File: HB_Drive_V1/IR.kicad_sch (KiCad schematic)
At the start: 57 parts, among them J301 Conn_02x03_Odd_Even, J303 Conn_01x02, J304 Conn_02x04_Odd_Even, U301 TL082, U302 TL082, U303 TL082, U304 TL082, U305 TL082

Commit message: updates board to REV 1 Ordered version
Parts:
- C301, C302: value 27uF 5% -> 27nF 5%
- C303: value 10uF 5% -> 10uF 10%
- R302, R308, R309, R310, R324, R325: value 10K -> 10kΩ 1%
- R307, R313, R316, R319, R322, R323, R326, R328, R329: value 10kΩ -> 10kΩ 1%
- R317: value 10KΩ -> 10kΩ 1%
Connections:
- net at R314.2, R318.2, TP301.1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: now also C301.1, R311.2
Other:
- moved on the sheet: TP301
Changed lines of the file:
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@@
 	)
 	(junction
+		(at 299.72 95.25)
+		(diameter 0)
+		(color 0 0 0 0)
+	)
+	(junction
 		(at 142.24 160.02)
 		(diameter 0)
@@
 	)
 	(junction
+		(at 325.12 107.95)
+		(diameter 0)
+		(color 0 0 0 0)
+	)
+	(junction
 		(at 124.46 160.02)
 		(diameter 0)
@@
 	(wire
 		(pts
+			(xy 299.72 95.25) (xy 320.04 95.25)
+		)
+		(stroke
+			(width 0)
+			(type default)
+		)
+	)
+	(wire
+		(pts
 			(xy 359.41 101.6) (xy 359.41 110.49)
 		)
@@
 	(wire
 		(pts
+			(xy 320.04 95.25) (xy 320.04 107.95)
+		)
+		(stroke
+			(width 0)
+			(type default)
+		)
+	)
+	(wire
+		(pts
 			(xy 314.96 78.74) (xy 331.47 78.74)
 		)
@@
 	(wire
 		(pts
+			(xy 325.12 107.95) (xy 330.2 107.95)
+		)
+		(stroke
+			(width 0)
+			(type default)
+		)
+	)
+	(wire
+		(pts
 			(xy 234.95 55.88) (xy 232.41 55.88)
 		)
@@
 	(wire
 		(pts
-			(xy 320.04 107.95) (xy 330.2 107.95)
+			(xy 320.04 107.95) (xy 325.12 107.95)
 		)
 		(stroke
@@
 			)
 		)
-		(property "Value" "10K"
+		(property "Value" "10kΩ 1%"
 			(at 129.794 101.6 90)
 			(hide yes)
@@
 			)
 		)
-		(property "Value" "10uF 5%"
+		(property "Value" "10uF 10%"
 			(at 309.118 69.85 90)
 			(show_name no)
@@
 			)
 		)
-		(property "Value" "10kΩ"
+		(property "Value" "10kΩ 1%"
 			(at 208.026 51.054 90)
 			(show_name no)
@@
 			)
 		)
-		(property "Value" "10kΩ"
-			(at 306.324 164.846 0)
+		(property "Value" "10kΩ 1%"
+			(at 308.356 164.846 0)
 			(show_name no)
 			(do_not_autoplace no)
@@
 			)
 		)
-		(property "Value" "10K"
+		(property "Value" "10kΩ 1%"
 			(at 292.354 173.99 90)
 			(hide yes)
@@
 			)
 		)
-		(property "Value" "27uF 5%"
+		(property "Value" "27nF 5%"
 			(at 292.1 99.06 90)
 			(show_name no)
@@
 			)
 		)
-		(property "Value" "10kΩ"
+		(property "Value" "10kΩ 1%"
 			(at 129.286 94.234 90)
 			(show_name no)
@@
 			)
 		)
-		(property "Value" "10K"
+		(property "Value" "10kΩ 1%"
 			(at 129.794 96.52 90)
 			(hide yes)
@@
 			)
 		)
-		(property "Value" "10kΩ"
+		(property "Value" "10kΩ 1%"
 			(at 152.146 89.154 90)
 			(show_name no)
@@
 			)
 		)
-		(property "Value" "10kΩ"
+		(property "Value" "10kΩ 1%"
 			(at 182.626 90.424 90)
 			(show_name no)
@@
 	(symbol
 		(lib_id "Connector:TestPoint")
-		(at 320.04 107.95 0)
+		(at 325.12 107.95 0)
 		(unit 1)
 		(body_style 1)
@@
 		(dnp no)
 		(property "Reference" "TP301"
-			(at 318.262 102.616 0)
+			(at 322.834 99.568 0)
 			(show_name no)
 			(do_not_autoplace no)
@@
 		)
 		(property "Value" "TestPoint"
-			(at 322.58 105.9179 0)
+			(at 327.66 105.9179 0)
 			(hide yes)
 			(show_name no)
@@
 		)
 		(property "Footprint" "TestPoint:TestPoint_Loop_D2.60mm_Drill1.6mm_Beaded"
-			(at 325.12 107.95 0)
+			(at 330.2 107.95 0)
 			(hide yes)
 			(show_name no)
@@
 		)
 		(property "Datasheet" ""
-			(at 325.12 107.95 0)
+			(at 330.2 107.95 0)
 			(hide yes)
 			(show_name no)
@@
 		)
 		(property "Description" "test point"
-			(at 320.04 107.95 0)
+			(at 325.12 107.95 0)
 			(hide yes)
 			(show_name no)
@@
 			)
 		)
-		(property "Value" "10K"
+		(property "Value" "10kΩ 1%"
 			(at 292.354 171.45 90)
 			(hide yes)
@@
 			)
 		)
-		(property "Value" "10KΩ"
+		(property "Value" "10kΩ 1%"
 			(at 163.576 52.832 90)
 			(hide yes)
@@
 			)
 		)
-		(property "Value" "27uF 5%"
+		(property "Value" "27nF 5%"
 			(at 292.1 109.22 90)
 			(show_name no)
@@
 			)
 		)
-		(property "Value" "10K"
+		(property "Value" "10kΩ 1%"
 			(at 273.304 41.91 90)
 			(show_name no)
@@
 			)
 		)
-		(property "Value" "10K"
+		(property "Value" "10kΩ 1%"
 			(at 129.794 99.06 90)
 			(hide yes)
@@
 			)
 		)
-		(property "Value" "10kΩ"
+		(property "Value" "10kΩ 1%"
 			(at 291.846 169.164 90)
 			(show_name no)
@@
 			)
 		)
-		(property "Value" "10kΩ"
+		(property "Value" "10kΩ 1%"
 			(at 224.536 43.434 90)
 			(show_name no)
@@
 			)
 		)
-		(property "Value" "10kΩ"
+		(property "Value" "10kΩ 1%"
 			(at 163.576 47.752 90)
 			(show_name no)
@@
 			)
 		)
-		(property "Value" "10kΩ"
+		(property "Value" "10kΩ 1%"
 			(at 167.386 96.774 90)
 			(show_name no)

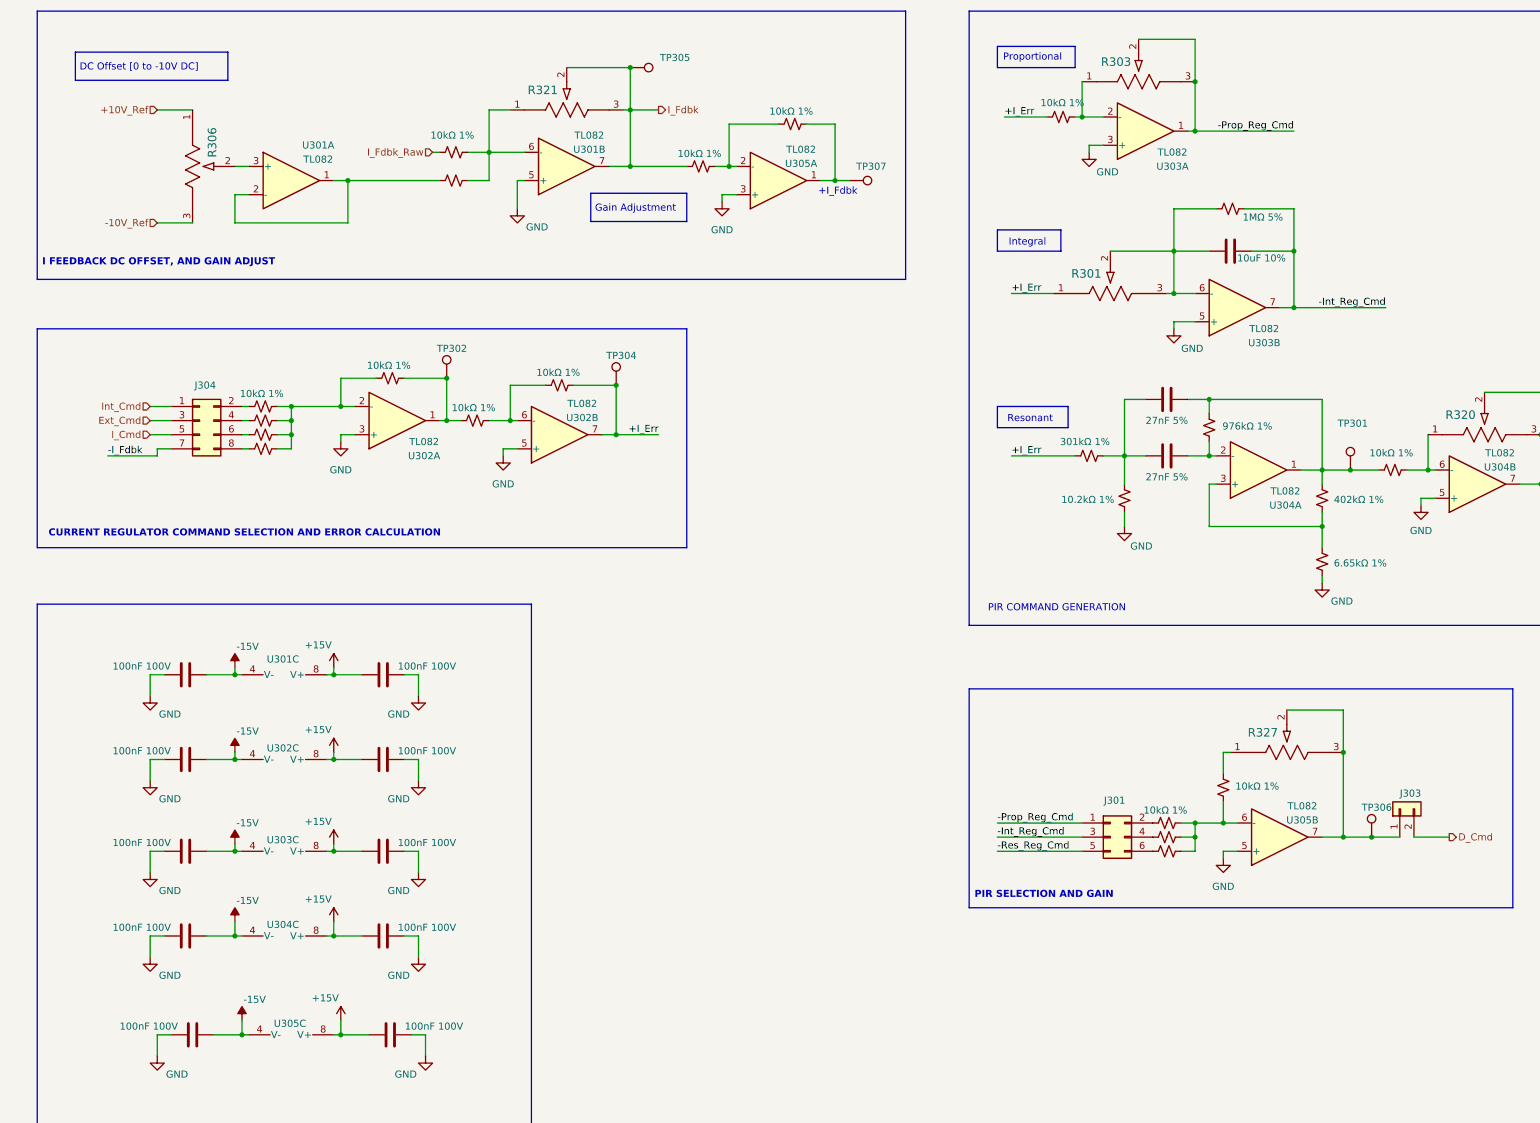
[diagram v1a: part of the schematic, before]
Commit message: Annotates Schematic! Fixes REV1 wiring swaps and replaces buffer
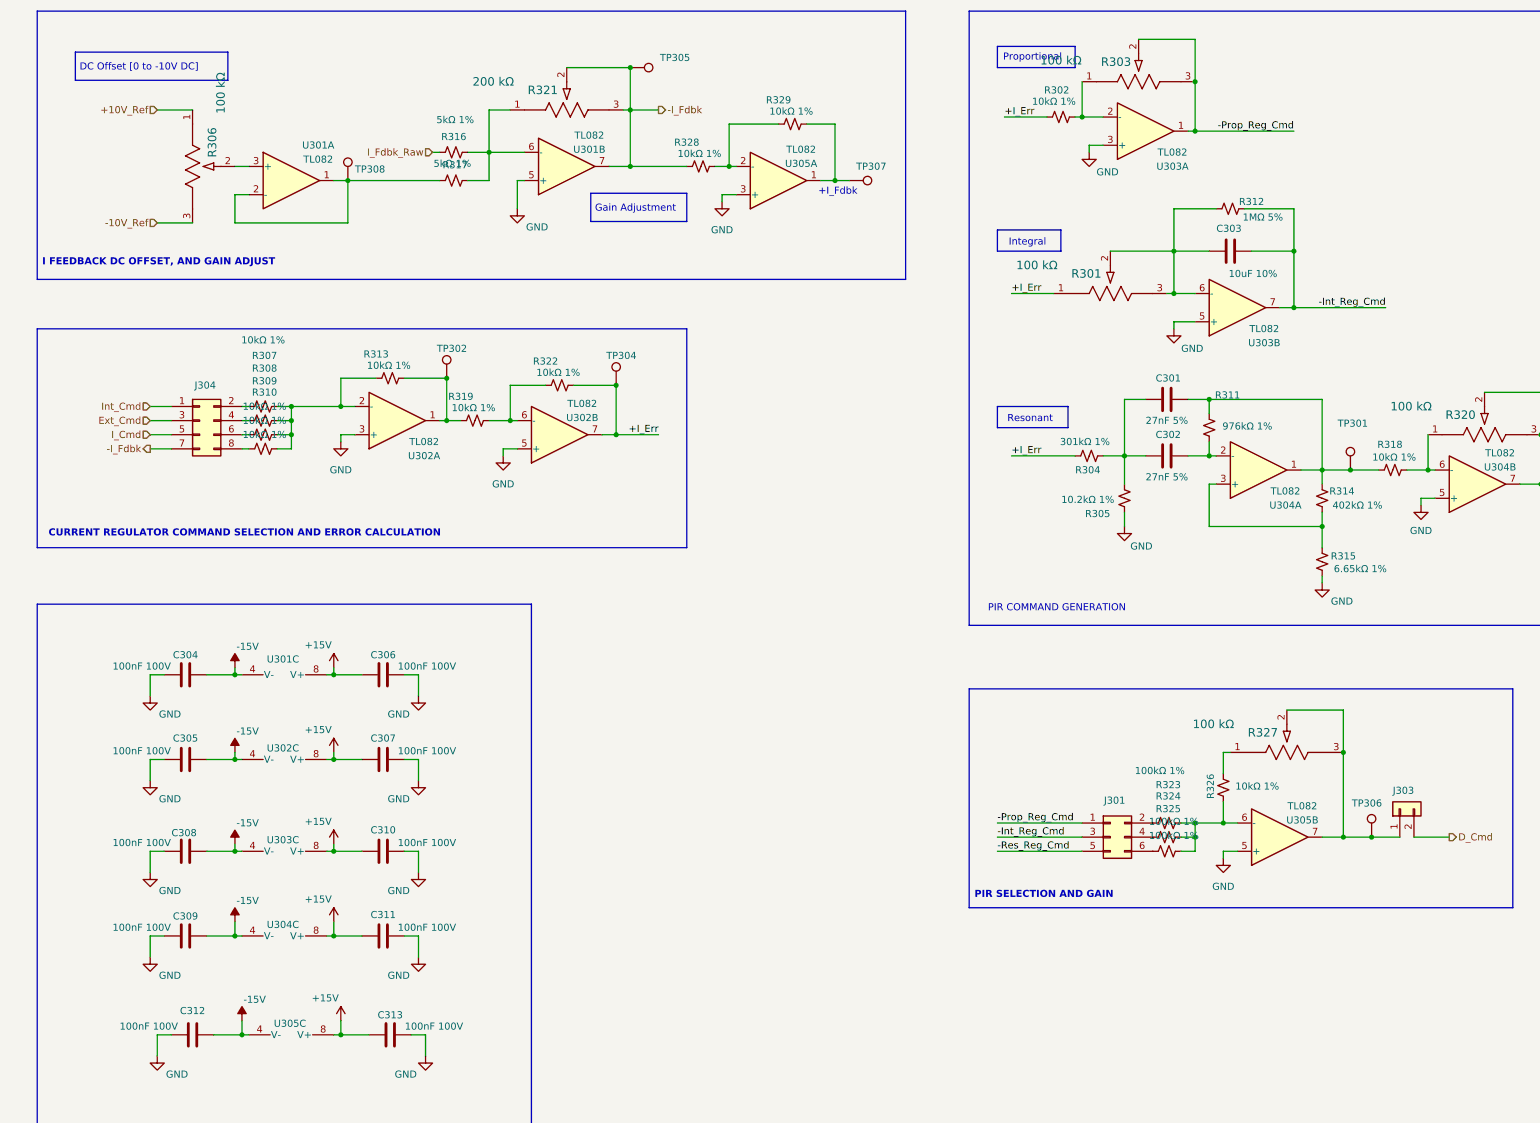
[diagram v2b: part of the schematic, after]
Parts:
- added TP308: TestPoint, TestPoint:TestPoint_Loop_D2.60mm_Drill1.6mm_Beaded, symbol Connector:TestPoint
- J303: footprint Connector_PinHeader_1.27mm:PinHeader_1x02_P1.27mm_Vertical -> Connector_PinHeader_2.54mm:PinHeader_1x02_P2.54mm_Vertical
- R301, R303, R306, R320, R327: value PV36W104C01B00 -> 100 kΩ
- R316, R317: value 10kΩ 1% -> 5kΩ 1%
- R321: value PV36W204C01B00 -> 200 kΩ
- R323, R324, R325: value 10kΩ 1% -> 100kΩ 1%
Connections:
- net I_Fdbk is gone; now on net -I_Fdbk: R321.2, R321.3, R328.2, TP305.1, U301.7
- net at R323.1, R326.1, U305.6 (-): now also R324.1, R325.1; no longer R324.2, R325.2
- net at J301.6 (Pin_6): now also R325.2; no longer R325.1
- net at J301.4 (Pin_4): now also R324.2; no longer R324.1
- net at R317.2, U301.1, U301.2 (-): now also TP308.1

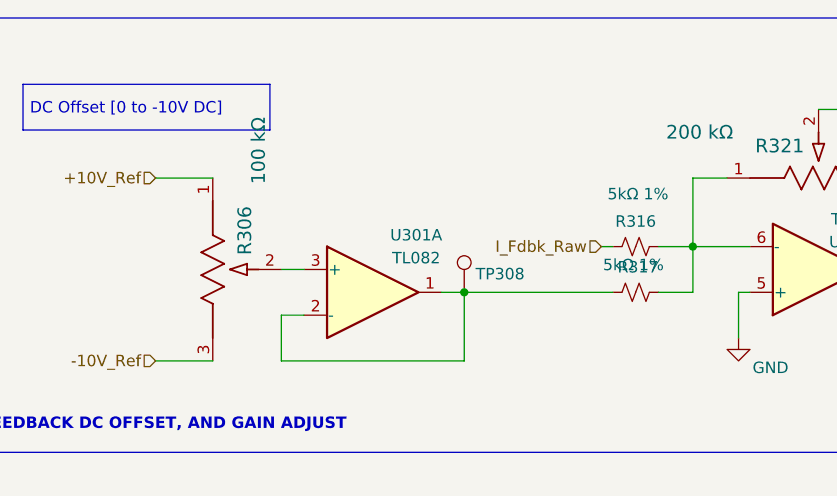
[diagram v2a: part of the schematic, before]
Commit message: annotates PCB! wiring is still broken here
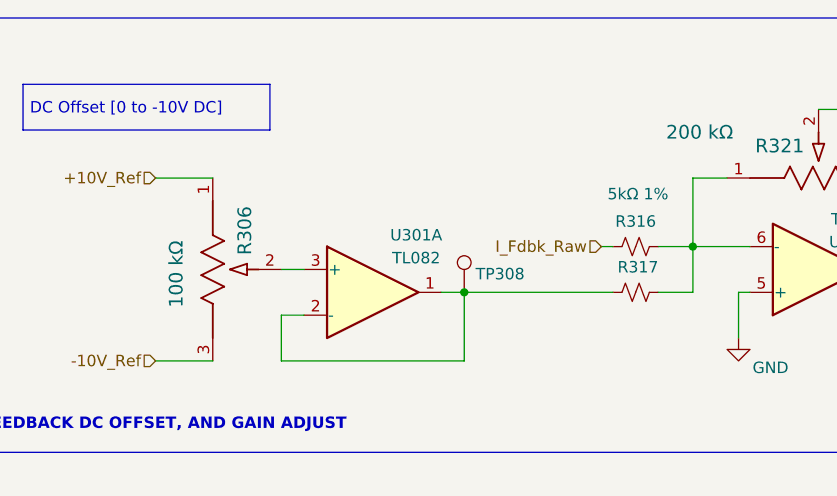
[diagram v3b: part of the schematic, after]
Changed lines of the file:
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@@
 		)
 		(property "Value" "5kΩ 1%"
-			(at 163.576 52.832 90)
+			(at 163.322 58.42 90)
+			(hide yes)
 			(show_name no)
 			(do_not_autoplace no)
@@
 		)
 		(property "Value" "100 kΩ"
-			(at 121.92 40.132 0)
-			(show_name no)
-			(do_not_autoplace no)
+			(at 112.776 53.848 0)
+			(show_name no)
+			(do_not_autoplace no)
